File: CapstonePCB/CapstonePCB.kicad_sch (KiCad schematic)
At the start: 43 parts, among them J1 Conn_02x40_Counter_Clockwise, J2 Barrel_Jack, J3 512964594, SW1 SW_Push, SW2 SW_Push, SW3 SW_Push, U1 NUCLEO64-F411RE, U2 LP-MSPM0G3507, U3 STSPIN220, U4 SN74AHC14N, U5 LM7805_TO220, U6 TLV1117-33, U7 COM-09032, U8 APDS-9306

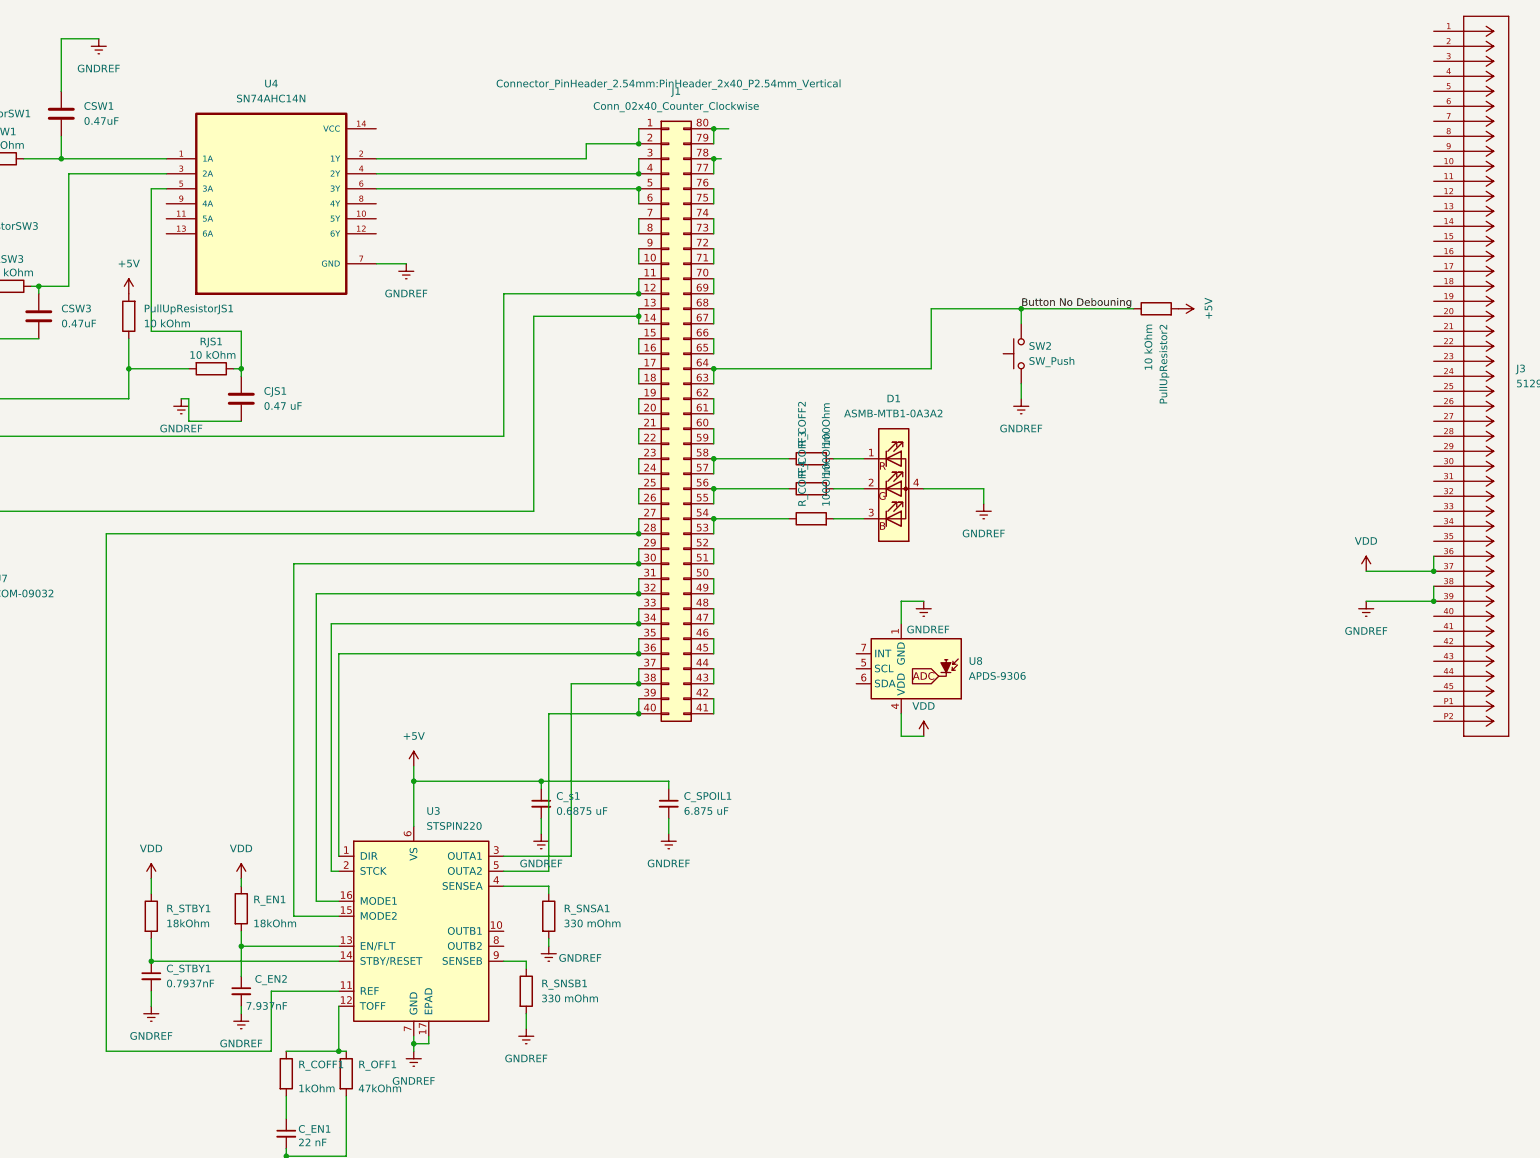
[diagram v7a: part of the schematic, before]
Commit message: Added power supply for LCD
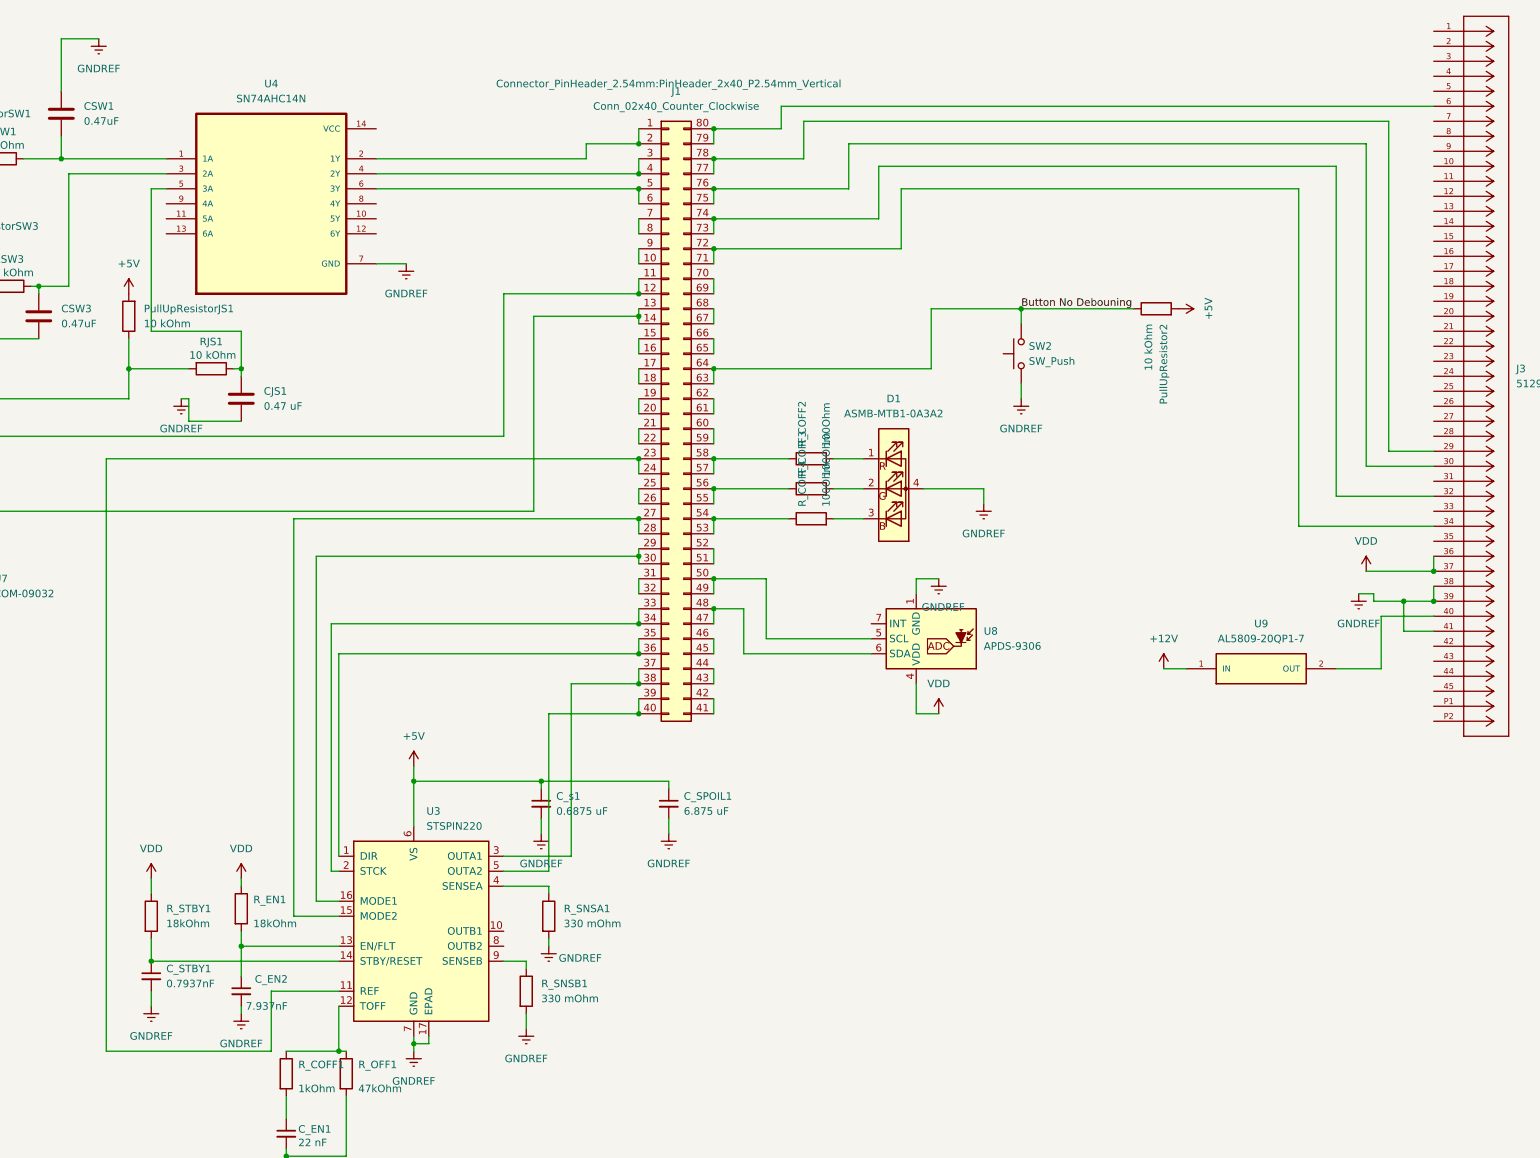
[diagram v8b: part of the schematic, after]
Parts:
- added U9: AL5809-20QP1-7, AL5809-20QP1-7:SODFL3717X100N, symbol AL5809-20QP1-7:AL5809-20QP1-7
- C_EN1, C_EN2, C_SPOIL1, C_STBY1, C_s1: footprint Capacitor_THT:C_Disc_D4.3mm_W1.9mm_P5.00mm -> Capacitor_SMD:C_0201_0603Metric
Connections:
- net +12V: now also U9.1 (IN)
- net GNDREF: now also J3.41
- net at U8.5 (SCL): now also J1.49 (Pin_49), J1.50 (Pin_50)
- net at U8.6 (SDA): now also J1.47 (Pin_47), J1.48 (Pin_48)
- net at J1.27 (Pin_27), J1.28 (Pin_28): now also U3.15 (MODE2); no longer U3.11 (REF)
- net at J1.29 (Pin_29), J1.30 (Pin_30): now also U3.16 (MODE1); no longer U3.15 (MODE2)
- net at J1.31 (Pin_31), J1.32 (Pin_32): no longer U3.16 (MODE1)
- net at J3.29: now also J1.77 (Pin_77), J1.78 (Pin_78)
- net at J3.30: now also J1.75 (Pin_75), J1.76 (Pin_76)
- net at J3.32: now also J1.73 (Pin_73), J1.74 (Pin_74)
- net at J3.34: now also J1.71 (Pin_71), J1.72 (Pin_72)
- net at J3.40: now also U9.2 (OUT)
- net at J3.6: now also J1.79 (Pin_79), J1.80 (Pin_80)
- net at J1.23 (Pin_23), J1.24 (Pin_24): now also U3.11 (REF)
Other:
- moved on the sheet: U8
